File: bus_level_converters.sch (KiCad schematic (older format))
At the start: 15 parts, among them U3 SN74ALVC164245DGG, U5 SN74ALVC164245DGG, U6 SN74ALVC164245DGG

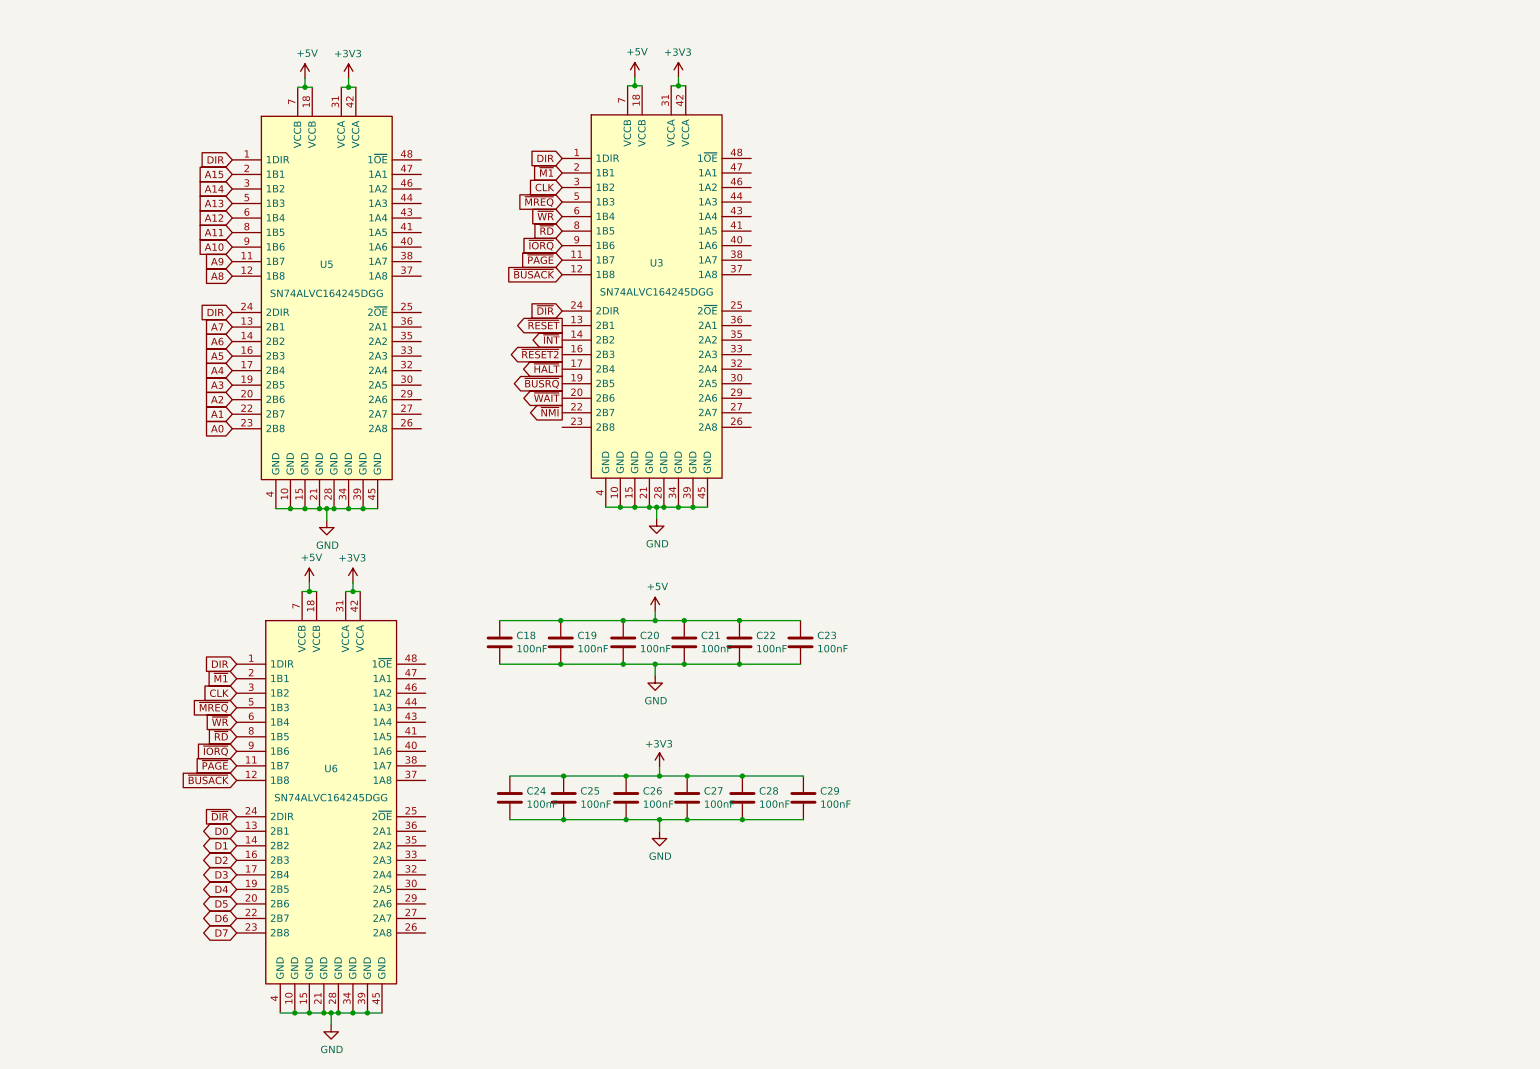
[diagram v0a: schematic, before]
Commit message: added FT JTAG
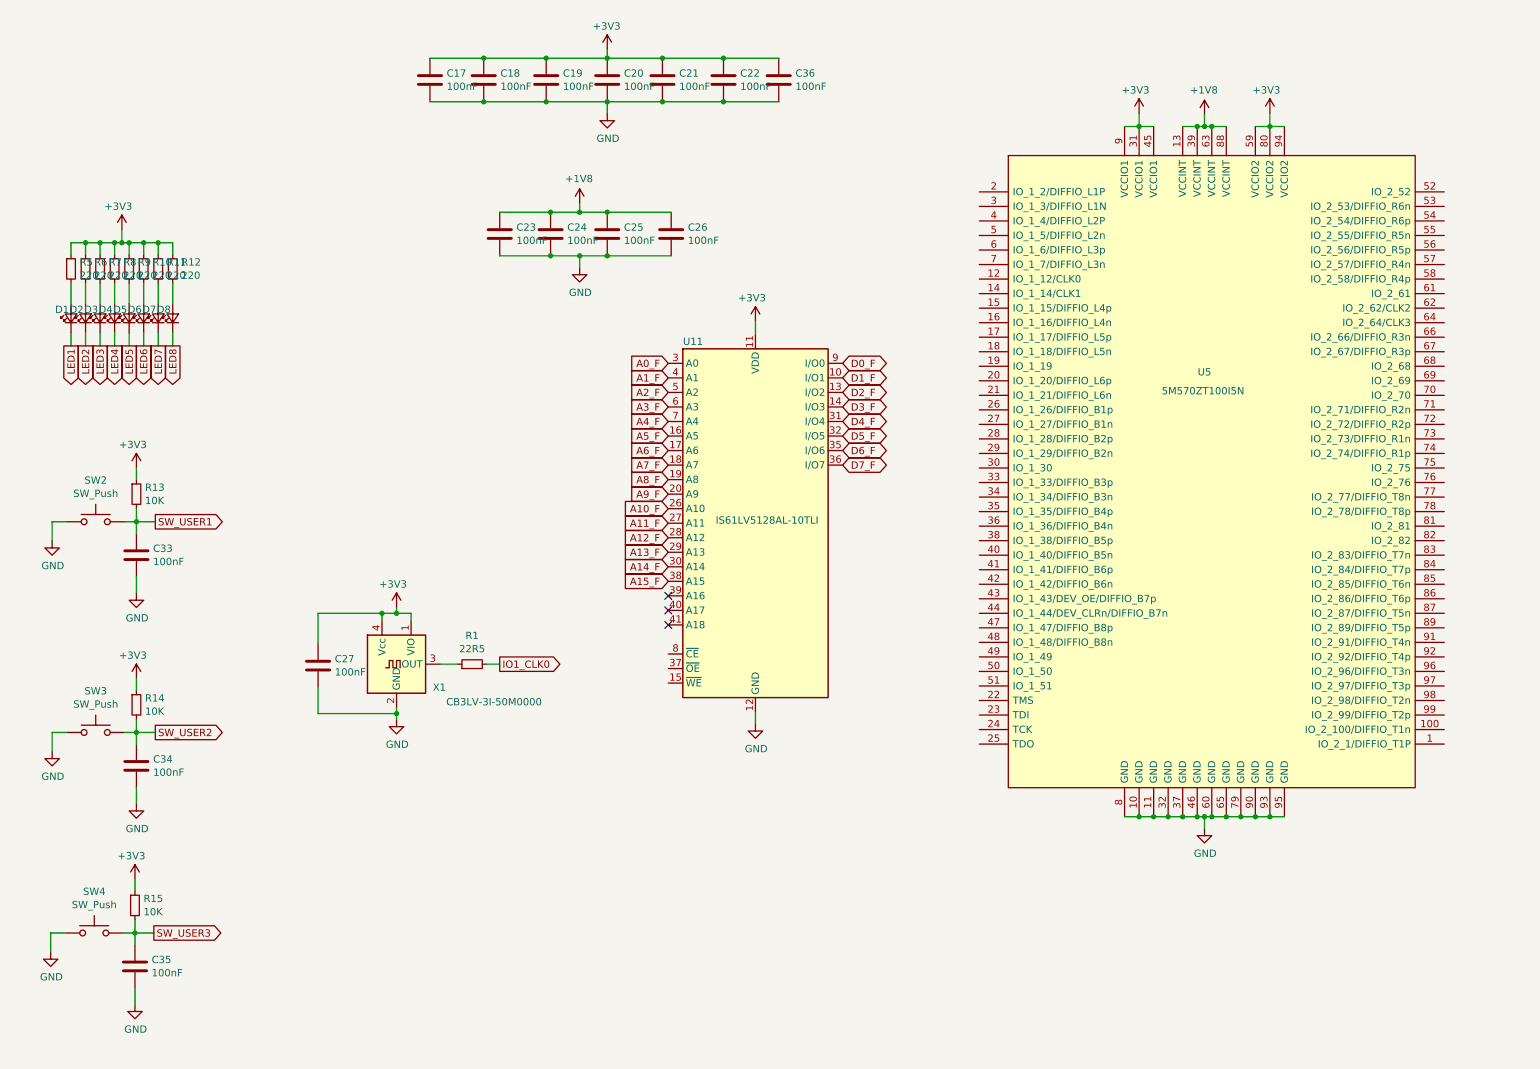
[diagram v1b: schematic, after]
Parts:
- removed C28, C29: 100nF, Capacitor_SMD:C_0603_1608Metric_Pad1.05x0.95mm_HandSolder, symbol Device:C
- removed U3, U5, U6: SN74ALVC164245DGG, Package_SO:TSSOP-48_6.1x12.5mm_P0.5mm, symbol rc2014_max_v-rescue:SN74ALVC164245DGG
- added C17, C33, C34, C35, C36: 100nF, Capacitor_SMD:C_0603_1608Metric_Pad1.05x0.95mm_HandSolder, symbol Device:C
- added D1, D2, D3, D4, D5, D6, D7, D8: Blue, LED_SMD:LED_0603_1608Metric_Pad1.05x0.95mm_HandSolder, symbol Device:LED_Small
- added R1: 22R5, Resistor_SMD:R_0603_1608Metric_Pad1.05x0.95mm_HandSolder, symbol Device:R_Small
- added R10, R11, R12, R5, R6, R7, R8, R9: 220, Resistor_SMD:R_0603_1608Metric_Pad1.05x0.95mm_HandSolder, symbol Device:R_Small
- added R13, R14, R15: 10K, Resistor_SMD:R_0603_1608Metric_Pad1.05x0.95mm_HandSolder, symbol Device:R_Small
- added SW2, SW3, SW4: SW_Push, Button_Switch_SMD:SW_SPST_CK_RS282G05A3, symbol Switch:SW_Push
- added U11: IS61LV5128AL-10TLI, Package_SO:TSOP-II-44_10.16x18.41mm_P0.8mm, symbol Memory_RAM:IS61LV5128AL-10TLI
- added U5: 5M570ZT100I5N, Package_QFP:TQFP-100_14x14mm_P0.5mm, symbol rc2014_max_v-rescue:5M570ZT100I5N
- added X1: CB3LV-3I-50M0000, Oscillator:Oscillator_SMD_SeikoEpson_SG8002CA-4Pin_7.0x5.0mm_HandSoldering, symbol Oscillator:CB3LV-3I-50M0000
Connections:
- net +3V3: now also C18.1, C19.1, C20.1, C21.1, C22.1, C17.1, C36.1, R10.1, R11.1, R12.1, R13.1, R14.1, R15.1, R5.1, R6.1, R7.1, R8.1, R9.1, U11.11 (VDD), U11.33 (VDD), U5.31 (VCCIO1), U5.45 (VCCIO1), U5.59 (VCCIO2), U5.80 (VCCIO2), U5.9 (VCCIO1), U5.94 (VCCIO2), X1.1 (VIO), X1.4 (Vcc); no longer C24.1, C25.1, C26.1
- net GND: now also C17.2, C33.2, C34.2, C35.2, C36.2, SW2.1, SW3.1, SW4.1, U11.12 (GND), U11.34 (GND), U5.10 (GND), U5.11 (GND), U5.32 (GND), U5.37 (GND), U5.46 (GND), U5.60 (GND), U5.65 (GND), U5.79 (GND), U5.8 (GND), U5.90 (GND), U5.93 (GND), U5.95 (GND), X1.2 (GND)
- removed net +5V: C18.1, C19.1, C20.1, C21.1, C22.1, C23.1
- new net: R1.1, X1.3 (OUT)
- new net: D1.2 (A), R5.2
- new net: D2.2 (A), R6.2
- new net: D3.2 (A), R7.2
- new net: D4.2 (A), R8.2
- new net: D5.2 (A), R9.2
- new net: D6.2 (A), R10.2
- new net: D7.2 (A), R11.2
- new net: D8.2 (A), R12.2
- new net +1V8: C23.1, C24.1, C25.1, C26.1, U5.13 (VCCINT), U5.39 (VCCINT), U5.63 (VCCINT), U5.88 (VCCINT)
- new net A0_F: U11.3 (A0)
- new net A10_F: U11.26 (A10)
- new net A11_F: U11.27 (A11)
- new net A12_F: U11.28 (A12)
- new net A13_F: U11.29 (A13)
- new net A14_F: U11.30 (A14)
- new net A15_F: U11.38 (A15)
- new net A1_F: U11.4 (A1)
- new net A2_F: U11.5 (A2)
- new net A3_F: U11.6 (A3)
- new net A4_F: U11.7 (A4)
- new net A5_F: U11.16 (A5)
- new net A6_F: U11.17 (A6)
- new net A7_F: U11.18 (A7)
- new net A8_F: U11.19 (A8)
- new net A9_F: U11.20 (A9)
- new net D0_F: U11.9 (I/O0)
- new net D1_F: U11.10 (I/O1)
- new net D2_F: U11.13 (I/O2)
- new net D3_F: U11.14 (I/O3)
- new net D4_F: U11.31 (I/O4)
- new net D5_F: U11.32 (I/O5)
- new net D6_F: U11.35 (I/O6)
- new net D7_F: U11.36 (I/O7)
- new net IO1_CLK0: R1.2
- new net LED1: D1.1 (K)
- new net LED2: D2.1 (K)
- new net LED3: D3.1 (K)
- new net LED4: D4.1 (K)
- new net LED5: D5.1 (K)
- new net LED6: D6.1 (K)
- new net LED7: D7.1 (K)
- new net LED8: D8.1 (K)
- new net SW_USER1: C33.1, R13.2, SW2.2
- new net SW_USER2: C34.1, R14.2, SW3.2
- new net SW_USER3: C35.1, R15.2, SW4.2
- no-connect marks 0 -> 3

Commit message: replaced single resistors with arrays
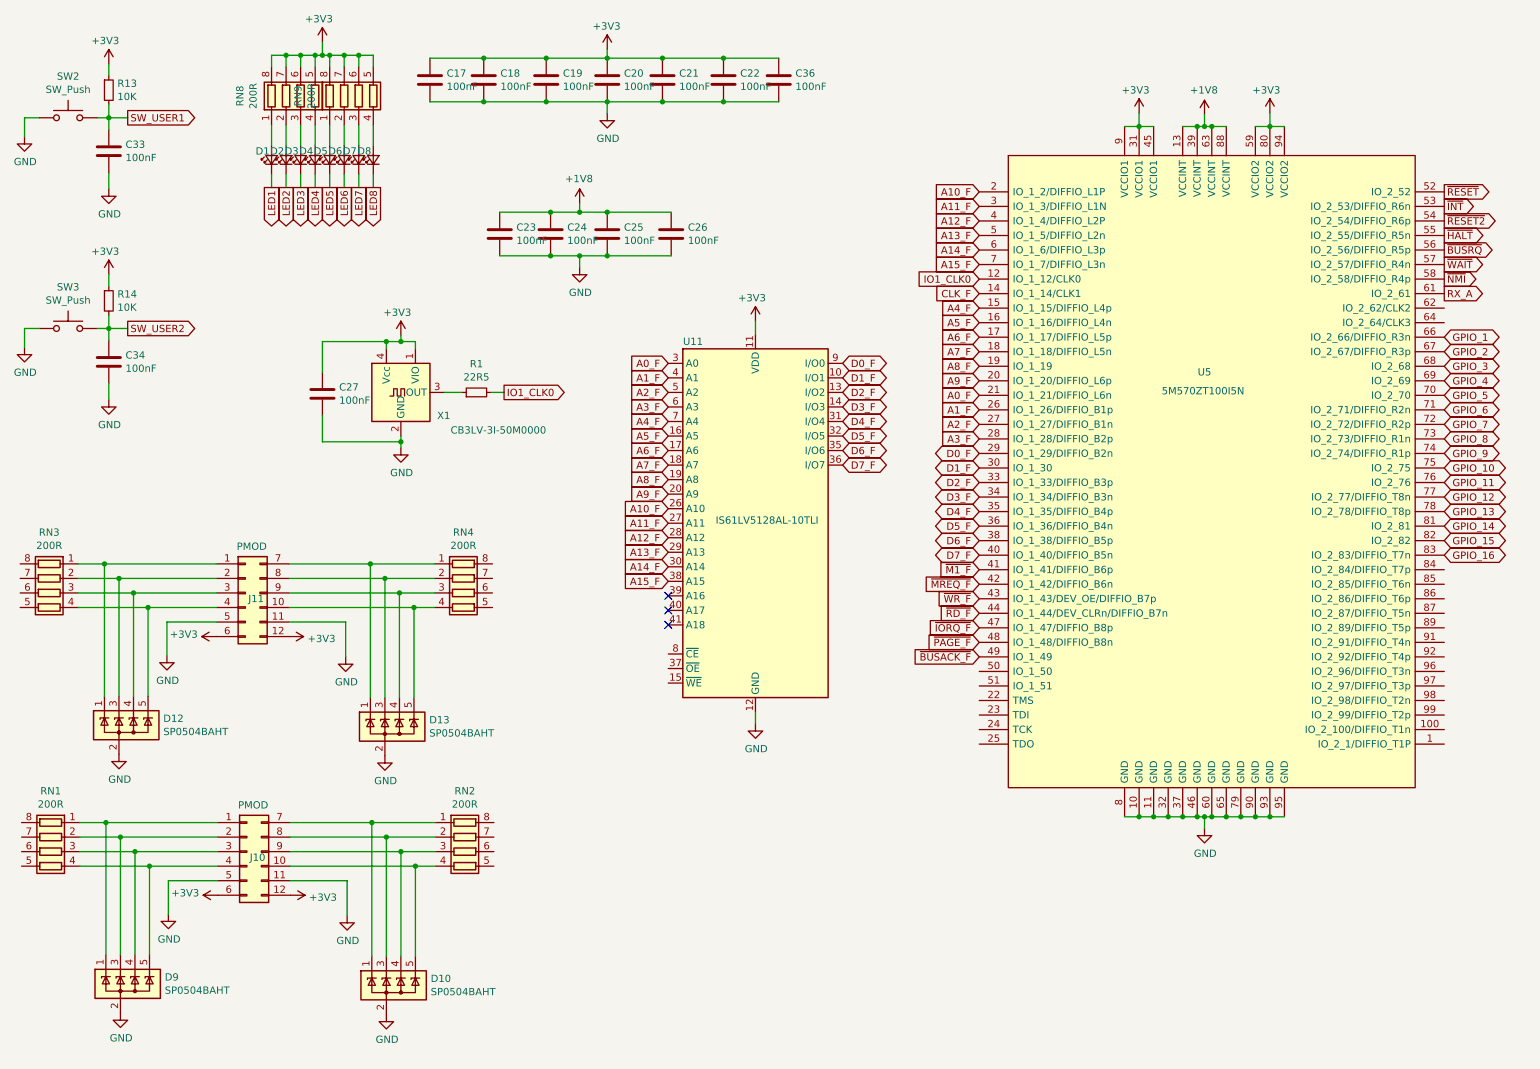
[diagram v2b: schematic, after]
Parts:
- removed C35: 100nF, Capacitor_SMD:C_0603_1608Metric_Pad1.05x0.95mm_HandSolder, symbol Device:C
- removed R10, R11, R12, R5, R6, R7, R8, R9: 220, Resistor_SMD:R_0603_1608Metric_Pad1.05x0.95mm_HandSolder, symbol Device:R_Small
- removed R15: 10K, Resistor_SMD:R_0603_1608Metric_Pad1.05x0.95mm_HandSolder, symbol Device:R_Small
- removed SW4: SW_Push, Button_Switch_SMD:SW_SPST_CK_RS282G05A3, symbol Switch:SW_Push
- added D10, D12, D13, D9: SP0504BAHT, Package_TO_SOT_SMD:SOT-23-5, symbol Power_Protection:SP0504BAHT
- added J10, J11: PMOD, Connector_PinSocket_2.54mm:PinSocket_2x06_P2.54mm_Horizontal, symbol Connector_Generic:Conn_02x06_Top_Bottom
- added RN1, RN2, RN3, RN4, RN8, RN9: 200R, Resistor_SMD:R_Array_Concave_4x0603, symbol Device:R_Pack04
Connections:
- net +3V3: now also J10.12 (Pin_12), J10.6 (Pin_6), J11.12 (Pin_12), J11.6 (Pin_6), RN8.5 (R4.2), RN8.6 (R3.2), RN8.7 (R2.2), RN8.8 (R1.2), RN9.5 (R4.2), RN9.6 (R3.2), RN9.7 (R2.2), RN9.8 (R1.2)
- net A0_F: now also U5.21 (IO_1_21/DIFFIO_L6n)
- net A10_F: now also U5.2 (IO_1_2/DIFFIO_L1P)
- net A11_F: now also U5.3 (IO_1_3/DIFFIO_L1N)
- net A12_F: now also U5.4 (IO_1_4/DIFFIO_L2P)
- net A13_F: now also U5.5 (IO_1_5/DIFFIO_L2n)
- net A14_F: now also U5.6 (IO_1_6/DIFFIO_L3p)
- net A15_F: now also U5.7 (IO_1_7/DIFFIO_L3n)
- net A1_F: now also U5.26 (IO_1_26/DIFFIO_B1p)
- net A2_F: now also U5.27 (IO_1_27/DIFFIO_B1n)
- net A3_F: now also U5.28 (IO_1_28/DIFFIO_B2p)
- net A4_F: now also U5.15 (IO_1_15/DIFFIO_L4p)
- net A5_F: now also U5.16 (IO_1_16/DIFFIO_L4n)
- net A6_F: now also U5.17 (IO_1_17/DIFFIO_L5p)
- net A7_F: now also U5.18 (IO_1_18/DIFFIO_L5n)
- net A8_F: now also U5.19 (IO_1_19)
- net A9_F: now also U5.20 (IO_1_20/DIFFIO_L6p)
- net D0_F: now also U5.29 (IO_1_29/DIFFIO_B2n)
- net D1_F: now also U5.30 (IO_1_30)
- net D2_F: now also U5.33 (IO_1_33/DIFFIO_B3p)
- net D3_F: now also U5.34 (IO_1_34/DIFFIO_B3n)
- net D4_F: now also U5.35 (IO_1_35/DIFFIO_B4p)
- net D5_F: now also U5.36 (IO_1_36/DIFFIO_B4n)
- net D6_F: now also U5.38 (IO_1_38/DIFFIO_B5p)
- net D7_F: now also U5.40 (IO_1_40/DIFFIO_B5n)
- net GND: now also D10.2 (A), D12.2 (A), D13.2 (A), D9.2 (A), J10.11 (Pin_11), J10.5 (Pin_5), J11.11 (Pin_11), J11.5 (Pin_5)
- net IO1_CLK0: now also U5.12 (IO_1_12/CLK0)
- net CLK_F: now reaches U5.14 (IO_1_14/CLK1)
- net ~M1_F: now reaches U5.41 (IO_1_41/DIFFIO_B6p)
- net ~MREQ_F: now reaches U5.42 (IO_1_42/DIFFIO_B6n)
- net ~WR_F: now reaches U5.43 (IO_1_43/DEV_OE/DIFFIO_B7p)
- net ~RD_F: now reaches U5.44 (IO_1_44/DEV_CLRn/DIFFIO_B7n)
- net ~IORQ_F: now reaches U5.47 (IO_1_47/DIFFIO_B8p)
- net ~PAGE_F: now reaches U5.48 (IO_1_48/DIFFIO_B8n)
- net ~BUSACK_F: now reaches U5.49 (IO_1_49)
- net ~RESET: now reaches U5.52 (IO_2_52)
- net ~INT: now reaches U5.53 (IO_2_53/DIFFIO_R6n)
- net ~RESET2: now reaches U5.54 (IO_2_54/DIFFIO_R6p)
- net ~HALT: now reaches U5.55 (IO_2_55/DIFFIO_R5n)
- net ~BUSRQ: now reaches U5.56 (IO_2_56/DIFFIO_R5p)
- net ~WAIT: now reaches U5.57 (IO_2_57/DIFFIO_R4n)
- net ~NMI: now reaches U5.58 (IO_2_58/DIFFIO_R4p)
- net RX_A: now reaches U5.61 (IO_2_61)
- net GPIO_1: now reaches U5.66 (IO_2_66/DIFFIO_R3n)
- net GPIO_2: now reaches U5.67 (IO_2_67/DIFFIO_R3p)
- net GPIO_3: now reaches U5.68 (IO_2_68)
- net GPIO_4: now reaches U5.69 (IO_2_69)
- net GPIO_5: now reaches U5.70 (IO_2_70)
- net GPIO_6: now reaches U5.71 (IO_2_71/DIFFIO_R2n)
- net GPIO_7: now reaches U5.72 (IO_2_72/DIFFIO_R2p)
- net GPIO_8: now reaches U5.73 (IO_2_73/DIFFIO_R1n)
- net GPIO_9: now reaches U5.74 (IO_2_74/DIFFIO_R1p)
- net GPIO_10: now reaches U5.75 (IO_2_75)
- net GPIO_11: now reaches U5.76 (IO_2_76)
- net GPIO_12: now reaches U5.77 (IO_2_77/DIFFIO_T8n)
- net GPIO_13: now reaches U5.78 (IO_2_78/DIFFIO_T8p)
- net GPIO_14: now reaches U5.81 (IO_2_81)
- net GPIO_15: now reaches U5.82 (IO_2_82)
- net GPIO_16: now reaches U5.83 (IO_2_83/DIFFIO_T7n)
- net at D1.2 (A): now also RN8.1 (R1.1)
- net at D2.2 (A): now also RN8.2 (R2.1)
- net at D3.2 (A): now also RN8.3 (R3.1)
- net at D4.2 (A): now also RN8.4 (R4.1)
- net at D5.2 (A): now also RN9.1 (R1.1)
- net at D6.2 (A): now also RN9.2 (R2.1)
- net at D7.2 (A): now also RN9.3 (R3.1)
- net at D8.2 (A): now also RN9.4 (R4.1)
- new net: D9.1 (K), J10.1 (Pin_1), RN1.1 (R1.1)
- new net: D9.3 (K), J10.2 (Pin_2), RN1.2 (R2.1)
- new net: D9.4 (K), J10.3 (Pin_3), RN1.3 (R3.1)
- new net: D9.5 (K), J10.4 (Pin_4), RN1.4 (R4.1)
- new net: D10.1 (K), J10.7 (Pin_7), RN2.1 (R1.1)
- new net: D10.3 (K), J10.8 (Pin_8), RN2.2 (R2.1)
- new net: D10.4 (K), J10.9 (Pin_9), RN2.3 (R3.1)
- new net: D10.5 (K), J10.10 (Pin_10), RN2.4 (R4.1)
- new net: D12.1 (K), J11.1 (Pin_1), RN3.1 (R1.1)
- new net: D12.3 (K), J11.2 (Pin_2), RN3.2 (R2.1)
- new net: D12.4 (K), J11.3 (Pin_3), RN3.3 (R3.1)
- new net: D12.5 (K), J11.4 (Pin_4), RN3.4 (R4.1)
- new net: D13.1 (K), J11.7 (Pin_7), RN4.1 (R1.1)
- new net: D13.3 (K), J11.8 (Pin_8), RN4.2 (R2.1)
- new net: D13.4 (K), J11.9 (Pin_9), RN4.3 (R3.1)
- new net: D13.5 (K), J11.10 (Pin_10), RN4.4 (R4.1)
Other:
- moved on the sheet: C27, C33, C34, D1, D2, D3, D4, D5, D6, D7, D8, R1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
